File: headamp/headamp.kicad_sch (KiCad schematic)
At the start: 0 parts

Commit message: headamp: schemat kanalu L zbudowany przez Konnect (KiCad) - ECC82 + EL84 trioda + OPT, S2, ERC 0 bledow
- U1A (1/2 ECC82) wspolna katoda, R3/C2 + S2/C3 (wokal do przodu)
- U2 EL84 ze zwora triodowa R9 100R, R8/C6, T1 SE 5k:80
- zarzenie: HEAT_A/HEAT_B (6,3V DC z common/), PWR_FLAG
- ERC: 0 bledow; ostrzezenia oczekiwane (wolny unit B ECC82 = kanal P, IN_L/OUT_L)

Co-Authored-By: Claude Fable 5 <noreply@anthropic.com>
Claude-Session: https://claude.ai/code/session_01TQb1FyUhGMrmgULtoCnCB2
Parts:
- added C1: 220n, symbol Device:C
- added C2: 1u/25V, symbol Device:C_Polarized
- added C3: 100u/25V, symbol Device:C_Polarized
- added C4: 47u/350V, symbol Device:C_Polarized
- added C5: 100n/400V, symbol Device:C
- added C6: 470u/25V, symbol Device:C_Polarized
- added R1, R6: 470k, symbol Device:R
- added R2, R7: 1k, symbol Device:R
- added R3: 1k5, symbol Device:R
- added R4: 47k/2W, symbol Device:R
- added R5: 10k/2W, symbol Device:R
- added R8: 270/5W, symbol Device:R
- added R9: 100, symbol Device:R
- added RV1: 50k log, symbol Device:R_Potentiometer
- added SW2: S2 wokal, symbol Switch:SW_SPST
- added T1: OPT SE 5k:80R (>=25H, 45mA), symbol Device:Transformer_1P_1S
- added U1: ECC82, symbol Valve:ECC81
- added U2: EL84 (trioda), symbol Valve:EL84
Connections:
- new net: R9.1, T1.2 (AB), U2.7 (A)
- new net: C1.2, R1.1, R2.1
- new net: R2.2, U1.7 (G)
- new net: C1.1, RV1.2
- new net: C2.1, R3.1, SW2.1 (A), U1.8 (K)
- new net: C6.1, R8.1, U2.3 (K_G3)
- new net: C4.1, R4.1, R5.1
- new net: C5.1, R4.2, U1.6 (A)
- new net: C5.2, R6.1, R7.1
- new net: R7.2, U2.2 (G1)
- new net: R9.2, U2.9 (G2)
- new net: C3.1, SW2.2 (B)
- new net +300V: R5.2, T1.1 (AA)
- new net GND: C2.2, C3.2, C4.2, C6.2, R1.2, R3.2, R6.2, R8.2, RV1.3, T1.3 (SA)
- new net HEAT_A: U1.4 (F1), U1.5 (F1), U2.4 (F1)
- new net HEAT_B: U1.9 (F2), U2.5 (F2)
- new net IN_L: RV1.1
- new net OUT_L: T1.4 (SB)

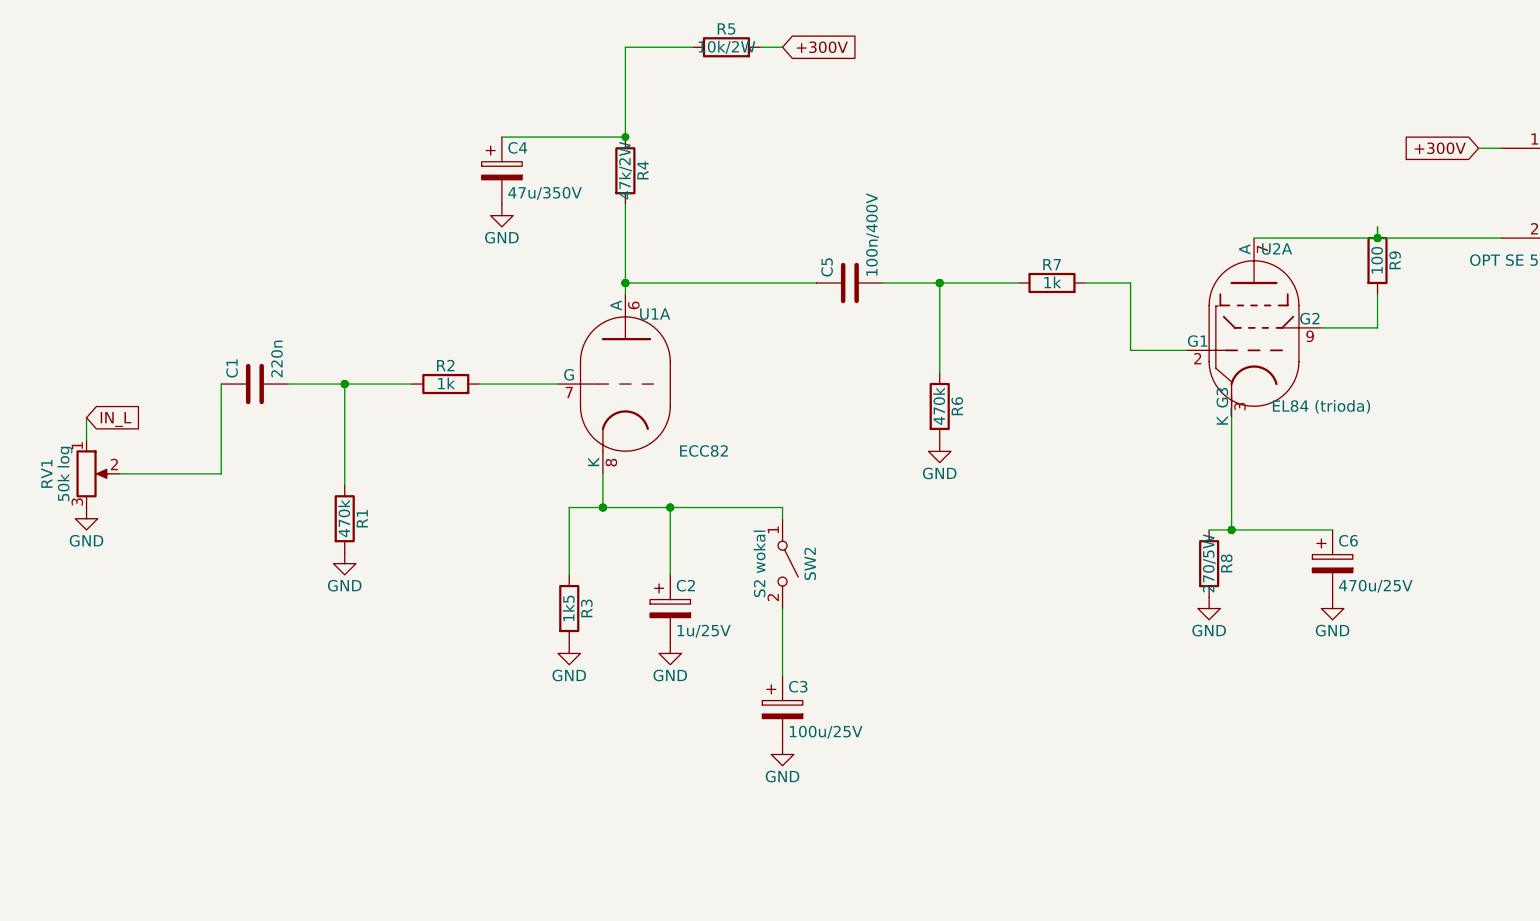
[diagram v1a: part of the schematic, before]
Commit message: headamp: tolerancje elementow pasywnych na schemacie (pole Tolerance)
Rezystory 5% (R3 1%), folie 5%, elektrolity i RV1 20%. Pola dodane przez
Konnect, widocznosc/pozycja skryptem (Konnect tego nie obsluguje). ERC 0.

Co-Authored-By: Claude Fable 5.1 <noreply@anthropic.com>
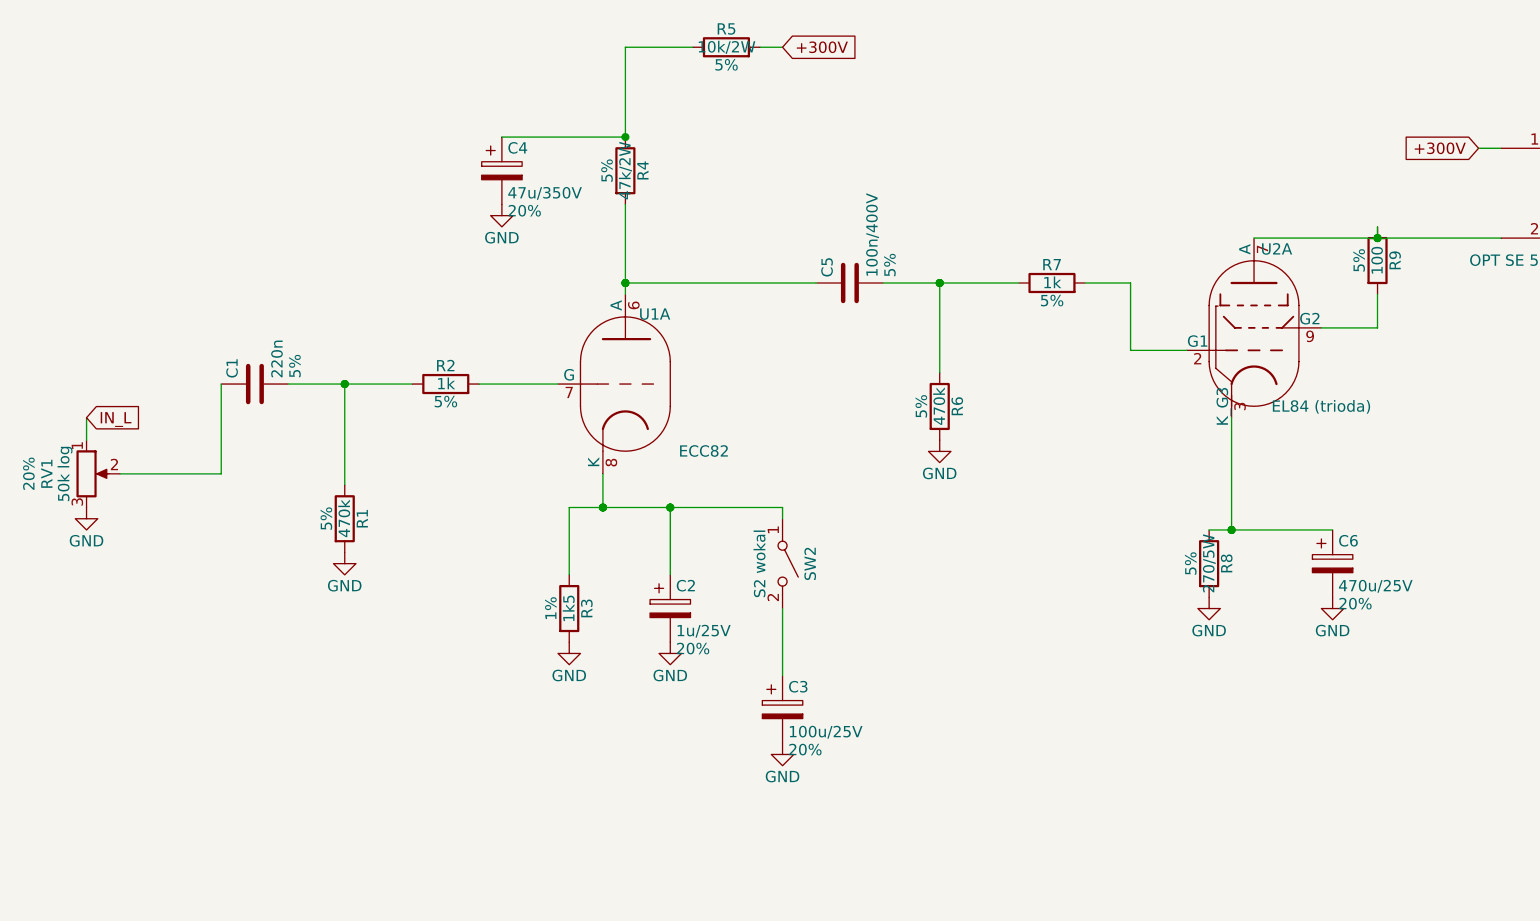
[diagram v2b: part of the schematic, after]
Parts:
- C1, C5, R1, R2, R4, R5, R6, R7, R8, R9: Tolerance (none) -> 5%
- C2, C3, C4, C6, RV1: Tolerance (none) -> 20%
- R3: Tolerance (none) -> 1%
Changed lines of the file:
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@@
+      )
+    )
+    (property "Tolerance" "20%"
+      (at 32.893 139.7 90)
+      (effects
+        (font
+          (size 1.27 1.27)
+        )
       )
     )
@@
       )
     )
+    (property "Tolerance" "5%"
+      (at 62.992 128.905 0)
+      (effects
+        (font
+          (size 1.27 1.27)
+        )
+        (justify left)
+      )
+    )
     (instances
       (project "headamp"
@@
       )
     )
+    (property "Tolerance" "5%"
+      (at 66.548 144.78 90)
+      (effects
+        (font
+          (size 1.27 1.27)
+        )
+      )
+    )
     (instances
       (project "headamp"
@@
       )
     )
+    (property "Tolerance" "5%"
+      (at 80.01 131.572 90)
+      (effects
+        (font
+          (size 1.27 1.27)
+        )
+      )
+    )
     (instances
       (project "headamp"
@@
       )
     )
+    (property "Tolerance" "1%"
+      (at 91.948 154.94 90)
+      (effects
+        (font
+          (size 1.27 1.27)
+        )
+      )
+    )
     (instances
       (project "headamp"
@@
       )
     )
+    (property "Tolerance" "20%"
+      (at 106.045 159.512 0)
+      (effects
+        (font
+          (size 1.27 1.27)
+        )
+        (justify left)
+      )
+    )
     (instances
       (project "headamp"
@@
       )
     )
+    (property "Tolerance" "20%"
+      (at 118.745 170.942 0)
+      (effects
+        (font
+          (size 1.27 1.27)
+        )
+        (justify left)
+      )
+    )
     (instances
       (project "headamp"
@@
       )
     )
+    (property "Tolerance" "5%"
+      (at 98.298 105.41 90)
+      (effects
+        (font
+          (size 1.27 1.27)
+        )
+      )
+    )
     (instances
       (project "headamp"
@@
       )
     )
+    (property "Tolerance" "20%"
+      (at 86.995 109.982 0)
+      (effects
+        (font
+          (size 1.27 1.27)
+        )
+        (justify left)
+      )
+    )
     (instances
       (project "headamp"
@@
       )
     )
+    (property "Tolerance" "5%"
+      (at 111.76 93.472 90)
+      (effects
+        (font
+          (size 1.27 1.27)
+        )
+      )
+    )
     (instances
       (project "headamp"
@@
       )
     )
+    (property "Tolerance" "5%"
+      (at 130.302 117.475 0)
+      (effects
+        (font
+          (size 1.27 1.27)
+        )
+        (justify left)
+      )
+    )
     (instances
       (project "headamp"
@@
       )
     )
+    (property "Tolerance" "5%"
+      (at 133.858 132.08 90)
+      (effects
+        (font
+          (size 1.27 1.27)
+        )
+      )
+    )
     (instances
       (project "headamp"
@@
       )
     )
+    (property "Tolerance" "5%"
+      (at 148.59 120.142 90)
+      (effects
+        (font
+          (size 1.27 1.27)
+        )
+      )
+    )
     (instances
       (project "headamp"
@@
       )
     )
+    (property "Tolerance" "5%"
+      (at 183.388 115.57 90)
+      (effects
+        (font
+          (size 1.27 1.27)
+        )
+      )
+    )
     (instances
       (project "headamp"
@@
       )
     )
+    (property "Tolerance" "5%"
+      (at 164.338 149.86 90)
+      (effects
+        (font
+          (size 1.27 1.27)
+        )
+      )
+    )
     (instances
       (project "headamp"
@@
       )
     )
+    (property "Tolerance" "20%"
+      (at 180.975 154.432 0)
+      (effects
+        (font
+          (size 1.27 1.27)
+        )
+        (justify left)
+      )
+    )

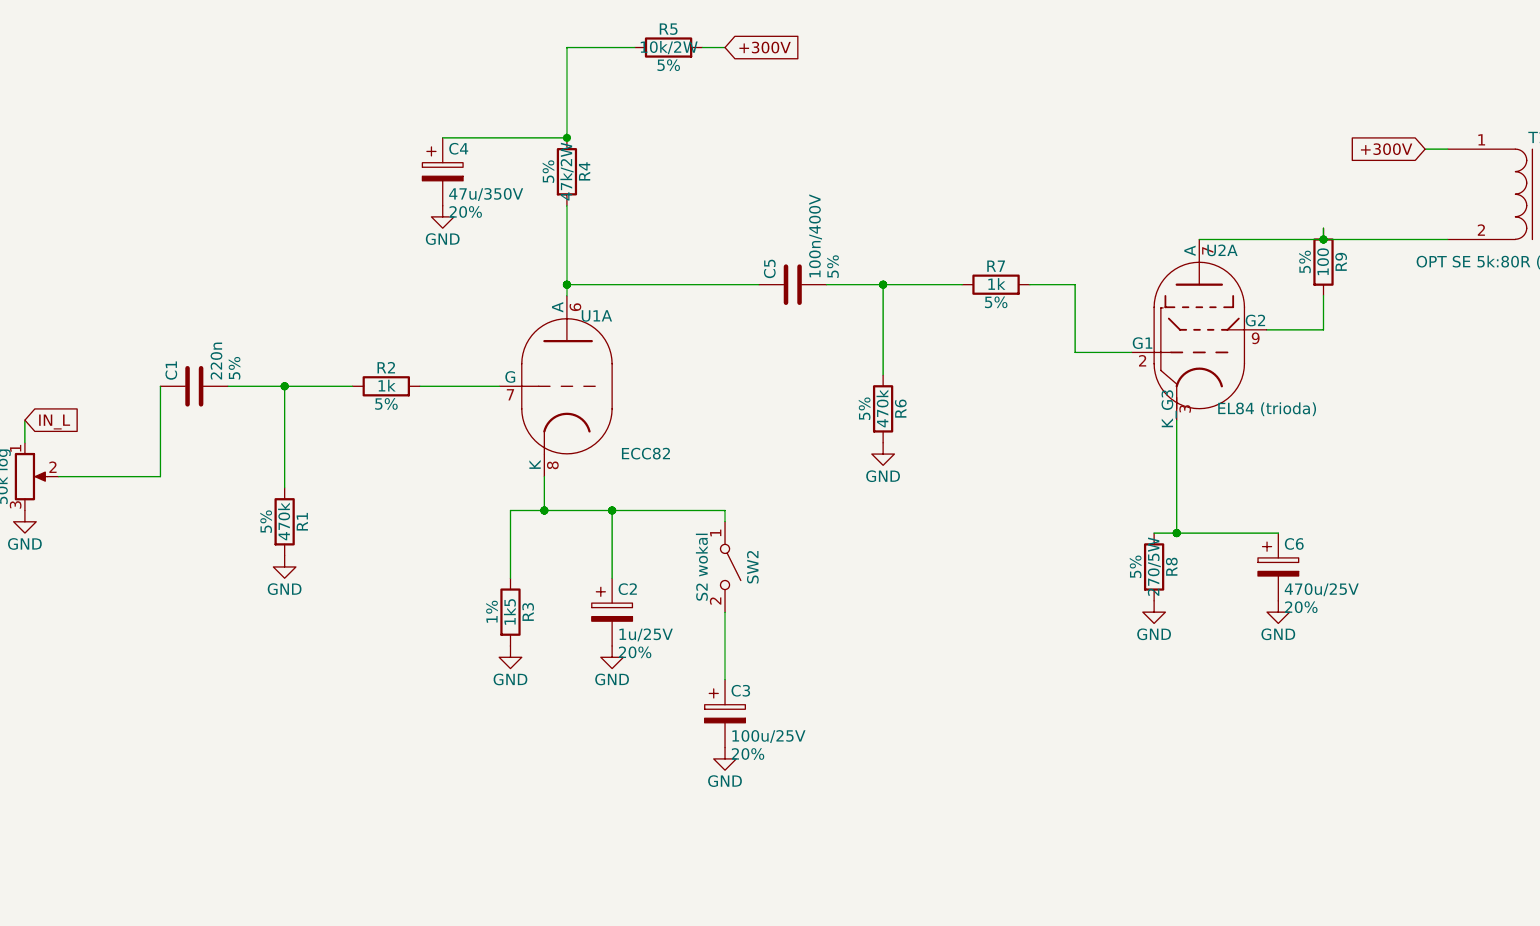
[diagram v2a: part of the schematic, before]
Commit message: headamp: generator schematu (gen.py + symlib.py + check.py), port kanalu L 1:1
Schemat kanalu L (audio + zarzenie) odtworzony jako kod (wzor riaa/gen.py)
z commitu b7d6cc9 (ERC 0 bledow). Netlista wygenerowanego pliku jest
rownowazna netliscie zrodlowej (te same partycje pin-do-pin, 18 sieci).
ERC po porcie: 5 ostrzezen (wolny unit B ECC82, dyndajace IN_L/OUT_L) -
identycznie jak przed portem. check.py z asercjami netlisty (wzor
riaa/check.py). headamp/headamp.kicad_sch jest teraz zrodlem
wygenerowanym przez gen.py, nie edytowac recznie w Eeschema.

Co-Authored-By: Claude Sonnet 5 <noreply@anthropic.com>
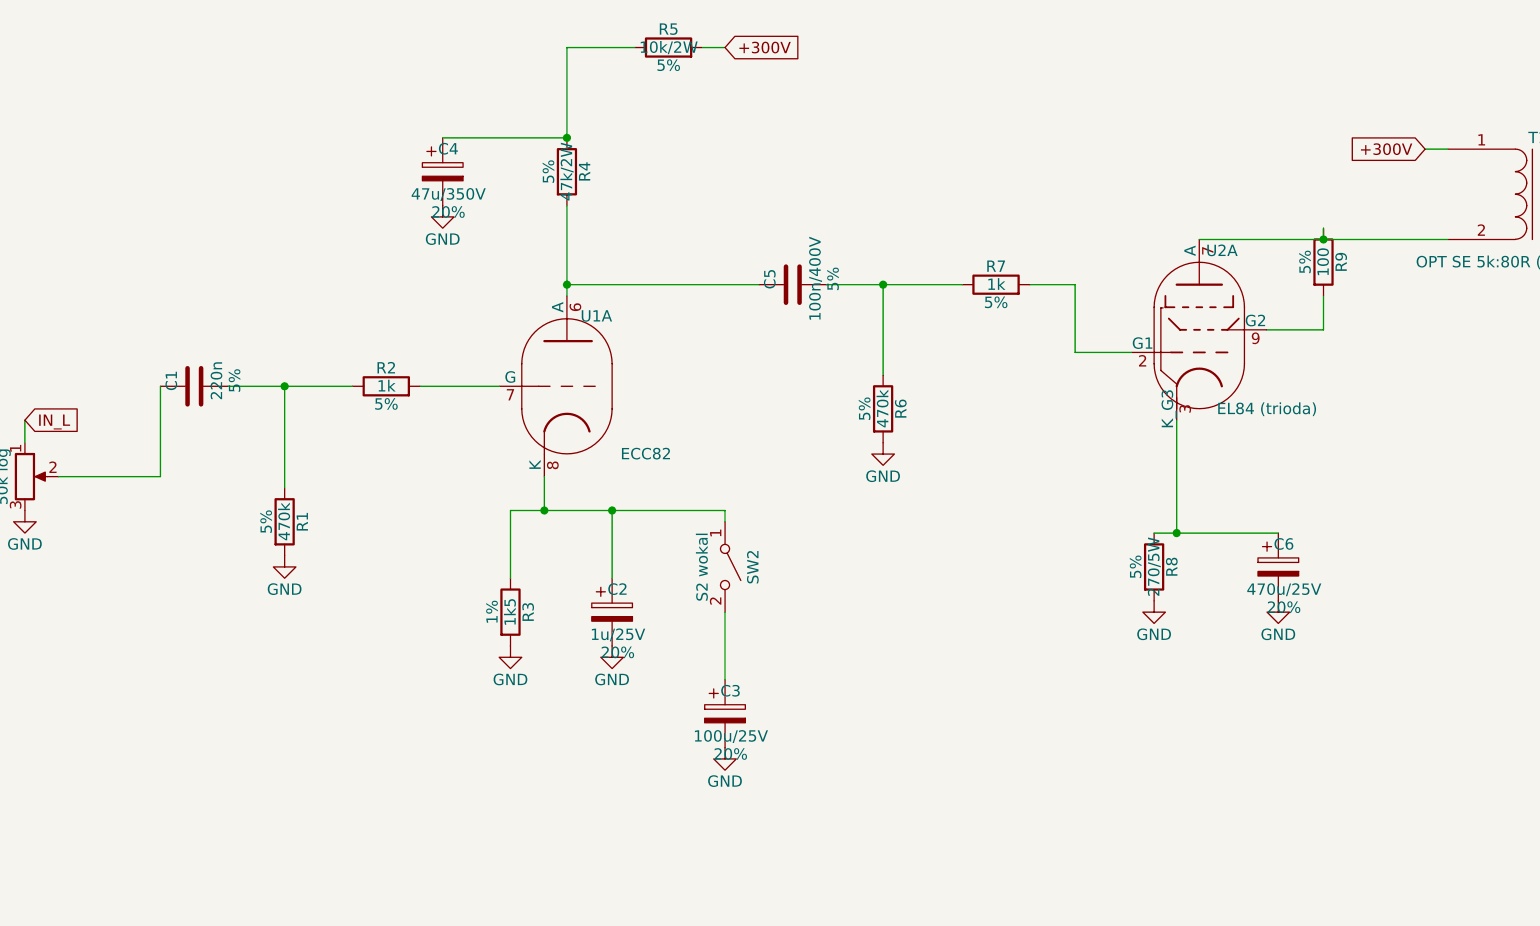
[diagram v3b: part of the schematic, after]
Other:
- title: TERCET headamp — SE EL84 (trioda) + 1/2 ECC82, OPT 5k:80 -> TERCET headamp - SE EL84 (trioda) + 1/2 ECC82, OPT 5k:80
